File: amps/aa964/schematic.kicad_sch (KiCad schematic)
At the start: 69 parts, among them SW1 AC sw, SW2 gnd sw

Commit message: Fix: the drawn tone stacks now are the tone stack the lab plots, and a gate says so
The tone-stack lab solves one network — the FMV stack documented in
site/src/lib/tonestack.js — and fills its values from each amp's BOM by
reference designator. Nothing checked that the schematic drew those
designators into that network, and nine of the nine drawings did not.

What the drawings said, rebuilt from the committed .kicad_sch files rather
than from the generators:

- 5F6-A, JTM45, 1987, 1959 and 5F4 ran the treble capacitor off the slope
  resistor's FOOT instead of the stack input, and landed the treble pot's
  lower lug on the bass-capacitor node instead of the slope foot.
- Every three-knob drawing left the bass pot's wiper unwired, so the plotted
  output (treble wiper AND bass wiper) existed on no drawing.
- JTM45, 1987 and 1959 put the mid capacitor in series with the mid pot down
  to ground rather than from the slope foot to the mid leg's top.
- 5F6 tied its bass pot as a rheostat and fed the mid capacitor to the middle
  pot's wiper.
- The blackface circuits left the treble pot's lower lug on the bass-cap node
  and tied the bass wiper to its own lug; AB763 drew its 0.047 µF inline on
  top of the bass pot's lug.

The 5F6-A's own layout.yaml — redrawn from the published Fender 5F6-A layout
sheet — already wires the canonical network (treble low to the slope node,
both wipers to the phase-inverter coupler), and 5F4's does too, so the
drawings were corrected to that rather than the lab to the drawings.

Consequences beyond the wires:

- 5F6-A's parts list prints one 0.02 µF line covering the bass and middle
  positions; the drawing showed one capacitor where the circuit has two.
  Added C5b with the same value and the same printed line cited. The plotted
  curve does not move — both positions already used that value.
- The blackface stacks keep the capacitor that feeds the mid leg. With the
  lug corrected, CBN/CB1 (0.1 µF) feeds the bass pot and CBN2/CB2 (0.047 µ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
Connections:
- net at VRT.2 (W), VRV.1: now also VRB.2 (W)
- net at CB1.2, VRB.1: no longer VRB.2 (W), VRT.3
- net at CB1.1, CB2.1, RS.2: now also VRT.3
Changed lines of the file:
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@@
   (wire (pts (xy 77.81 56.9) (xy 84 56.9))
+    (stroke (width 0) (type default)))
+  (wire (pts (xy 96 50.52) (xy 84 50.52))
+    (stroke (width 0) (type default)))
+  (wire (pts (xy 84 50.52) (xy 84 56.9))
     (stroke (width 0) (type default)))
   (symbol (lib_id "cx:C") (at 90 56.9 90) (unit 1)
@@
   (wire (pts (xy 93.81 56.9) (xy 96 56.9))
     (stroke (width 0) (type default)))
-  (wire (pts (xy 96 50.52) (xy 96 56.9))
-    (stroke (width 0) (type default)))
   (symbol (lib_id "cx:POT") (at 96 60.71 0) (unit 1)
     (in_bom yes) (on_board yes)
     (property "Reference" "VRB" (at 98.2 57.51 0) (effects (font (size 1.27 1.27)) (justify left)))
     (property "Value" "250k bass" (at 98.2 59.91 0) (effects (font (size 1.27 1.27)) (justify left))))
-  (junction (at 96 56.9) (diameter 0) (color 0 0 0 0))
-  (wire (pts (xy 101.08 60.71) (xy 105 60.71))
+  (wire (pts (xy 101.08 60.71) (xy 108 60.71))
     (stroke (width 0) (type default)))
-  (wire (pts (xy 105 60.71) (xy 105 53.9))
+  (wire (pts (xy 108 60.71) (xy 108 46.71))
     (stroke (width 0) (type default)))
-  (wire (pts (xy 105 53.9) (xy 96 53.9))
-    (stroke (width 0) (type default)))
-  (junction (at 96 53.9) (diameter 0) (color 0 0 0 0))
+  (junction (at 108 46.71) (diameter 0) (color 0 0 0 0))
   (wire (pts (xy 84 56.9) (xy 84 64.52))
     (stroke (width 0) (type default)))

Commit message: Fix: the published sheets draw a different tone stack, and now we draw theirs
The tone-stack pass rewired nine schematics to one "canonical FMV" network —
treble lower lug on the slope foot, treble and bass wipers joined at the
output, mid cap on a rheostat-wired mid pot — on the strength of the 5F6-A
layout.yaml, a redraw that omits the tone capacitors "for legibility" and
whose stack runs were convention, not sheet reading. Fetching the published
drawings and reading them settles what they actually draw, and it is not that
network. Five sheets were read at 300-400 dpi:

- Fender 5F6 (F-EG), schematic AND factory layout pages
- Fender 5F6-A (I-EG), schematic and layout, side by side
- Marshall JTM45 trem ('types 1961, 1962, 1987/T'), Unicord 70-19-11 (1987),
  and the 100 W Type #2 c.1967 (1959)
- Fender Princeton AA964, schematic and factory layout

All of them agree on a ladder: the treble cap and the slope resistor both
leave the stack input; the first bass cap lands on the node shared by the
treble pot's LOWER lug and the bass pot — the treble pot's cold end sits on
the far side of that capacitor, not on the slope foot; the bass pot is a
rheostat (arrow-through-body on most sheets; the JTM45 loops its wiper to the
foot lug, the 5F6 factory layout straps it into the treble-lug node) in
series down the ladder; the mid cap feeds the MIDDLE POT'S WIPER, not its
top; and the stack's output is the treble wiper ALONE. The blackface AA964
draws the same ladder with its 6.8k fixed leg. The 5F6's presence-in-the-
ground-leg arrangement is unchanged and was always right.

So five drawings return to their sheets: 5f6 and aa964 revert to their
pre-rewire wiring (which the extractor confirms matched the sheets all
along), and jtm45/m1987/m1959 are redrawn to the sheets outright — their old
drawings were wrong differently (treble cap off the slope foot, mid cap in
series to ground, bass wiper floating), so neither old nor "canonical" would
do.

The lab keeps all five as prese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
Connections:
- net at CB1.1, CB2.1, RS.2: no longer VRT.3
- net at CB1.2, VRB.1: now also VRB.2 (W), VRT.3
- net at VRT.2 (W), VRV.1: no longer VRB.2 (W)
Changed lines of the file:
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@@
   (wire (pts (xy 77.81 56.9) (xy 84 56.9))
-    (stroke (width 0) (type default)))
-  (wire (pts (xy 96 50.52) (xy 84 50.52))
-    (stroke (width 0) (type default)))
-  (wire (pts (xy 84 50.52) (xy 84 56.9))
     (stroke (width 0) (type default)))
   (symbol (lib_id "cx:C") (at 90 56.9 90) (unit 1)
@@
   (wire (pts (xy 93.81 56.9) (xy 96 56.9))
     (stroke (width 0) (type default)))
+  (wire (pts (xy 96 50.52) (xy 96 56.9))
+    (stroke (width 0) (type default)))
   (symbol (lib_id "cx:POT") (at 96 60.71 0) (unit 1)
     (in_bom yes) (on_board yes)
@@
   (wire (pts (xy 101.08 60.71) (xy 108 60.71))
     (stroke (width 0) (type default)))
-  (wire (pts (xy 108 60.71) (xy 108 46.71))
+  (wire (pts (xy 108 60.71) (xy 108 56.9))
     (stroke (width 0) (type default)))
-  (junction (at 108 46.71) (diameter 0) (color 0 0 0 0))
+  (wire (pts (xy 108 56.9) (xy 96 56.9))
+    (stroke (width 0) (type default)))
+  (junction (at 96 56.9) (diameter 0) (color 0 0 0 0))
   (wire (pts (xy 84 56.9) (xy 84 64.52))
     (stroke (width 0) (type default)))

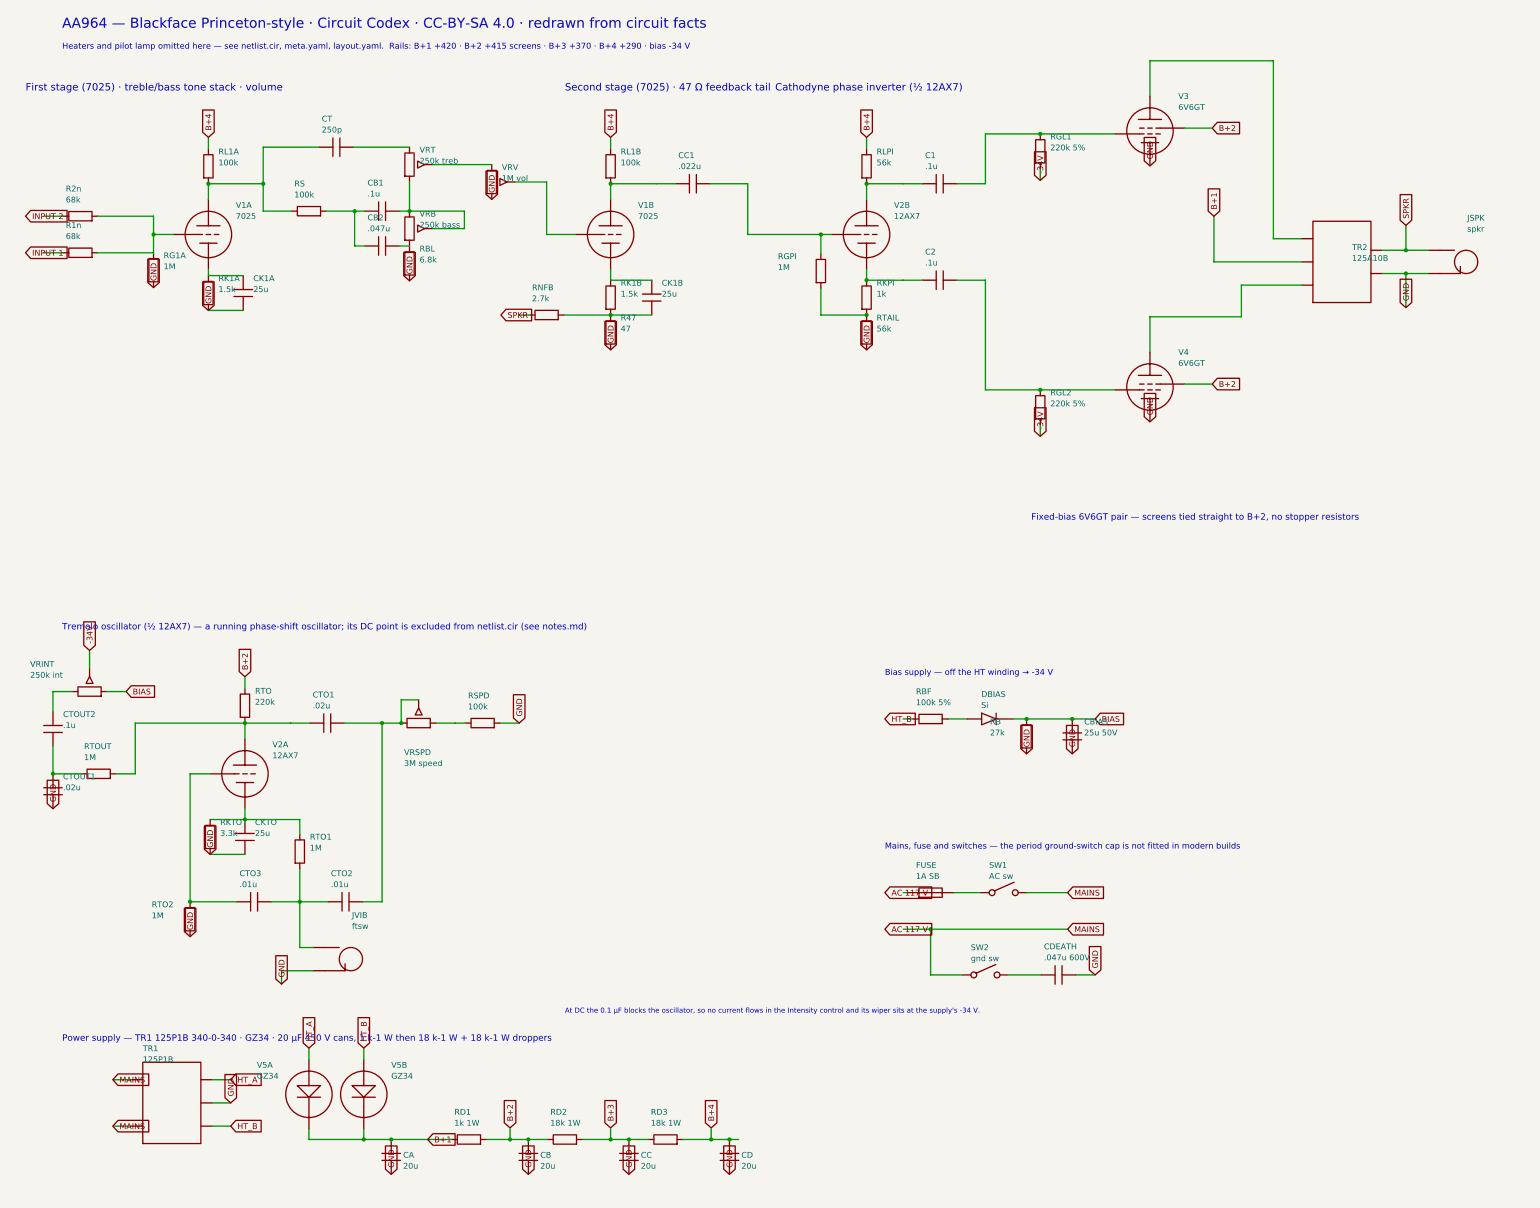
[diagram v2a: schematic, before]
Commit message: Fix: schematic sheets — real title block, fitted paper, no lettering through circuitry
Every sheet in the corpus shipped with an EMPTY title block ("Title:" and
"Date:" blank, default "Sheet /" furniture) laid onto a fixed A4/A3 page
regardless of the drawing's size, with prose annotations placed by hand
wherever a coordinate looked free when the amp was first drawn. The result
read as an unfinished alpha under a `verified` badge: KiCanvas's default view
is `zoom_to_page()`, so a 150 x 110 mm circuit on an A3 sheet opened as a
postage stamp, and later edits had pushed live circuitry under the prose.

schematic_lib.py — the builder now records each element as a (kind, points,
extra) tuple instead of a finished string, so `write()` can measure and move
what it emits:

- emits a real `(title_block …)` read from the amp's own meta.yaml — Title =
  designation + style, Date = the verification (or added) date, Rev = the
  verification status, Company = Circuit Codex, plus the licence and source
  URL as comments. Fixes all 34 sheets from one place;
- emits `(paper "User" w h)` cut to the drawing, translated to a fixed margin,
  with the bottom 34 mm strip reserved for the worksheet's title block. Sheet
  utilisation of the drawable area went from as low as ~20% to 92-98%;
- `note()` queues prose into a wrapped band under the circuit, and `caption()`
  places a section heading over the block it names, nudging it clear if it
  would print through anything;
- per-symbol default label offsets (the old single default printed every pot's
  value through its own wiper arrow and every transformer's designator through
  its body), plus `place_labels()`, which moves any designator/value block that
  would print over ink;
- transformers and chokes are drawn, not boxed: iron core between two windings,
  centre taps where the part has them, and an optional `spec` lettering slot for
  a ratio or impedance;
- `gnd()` takes a direction, because a flag defaulting to "down" at the HEAD of
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
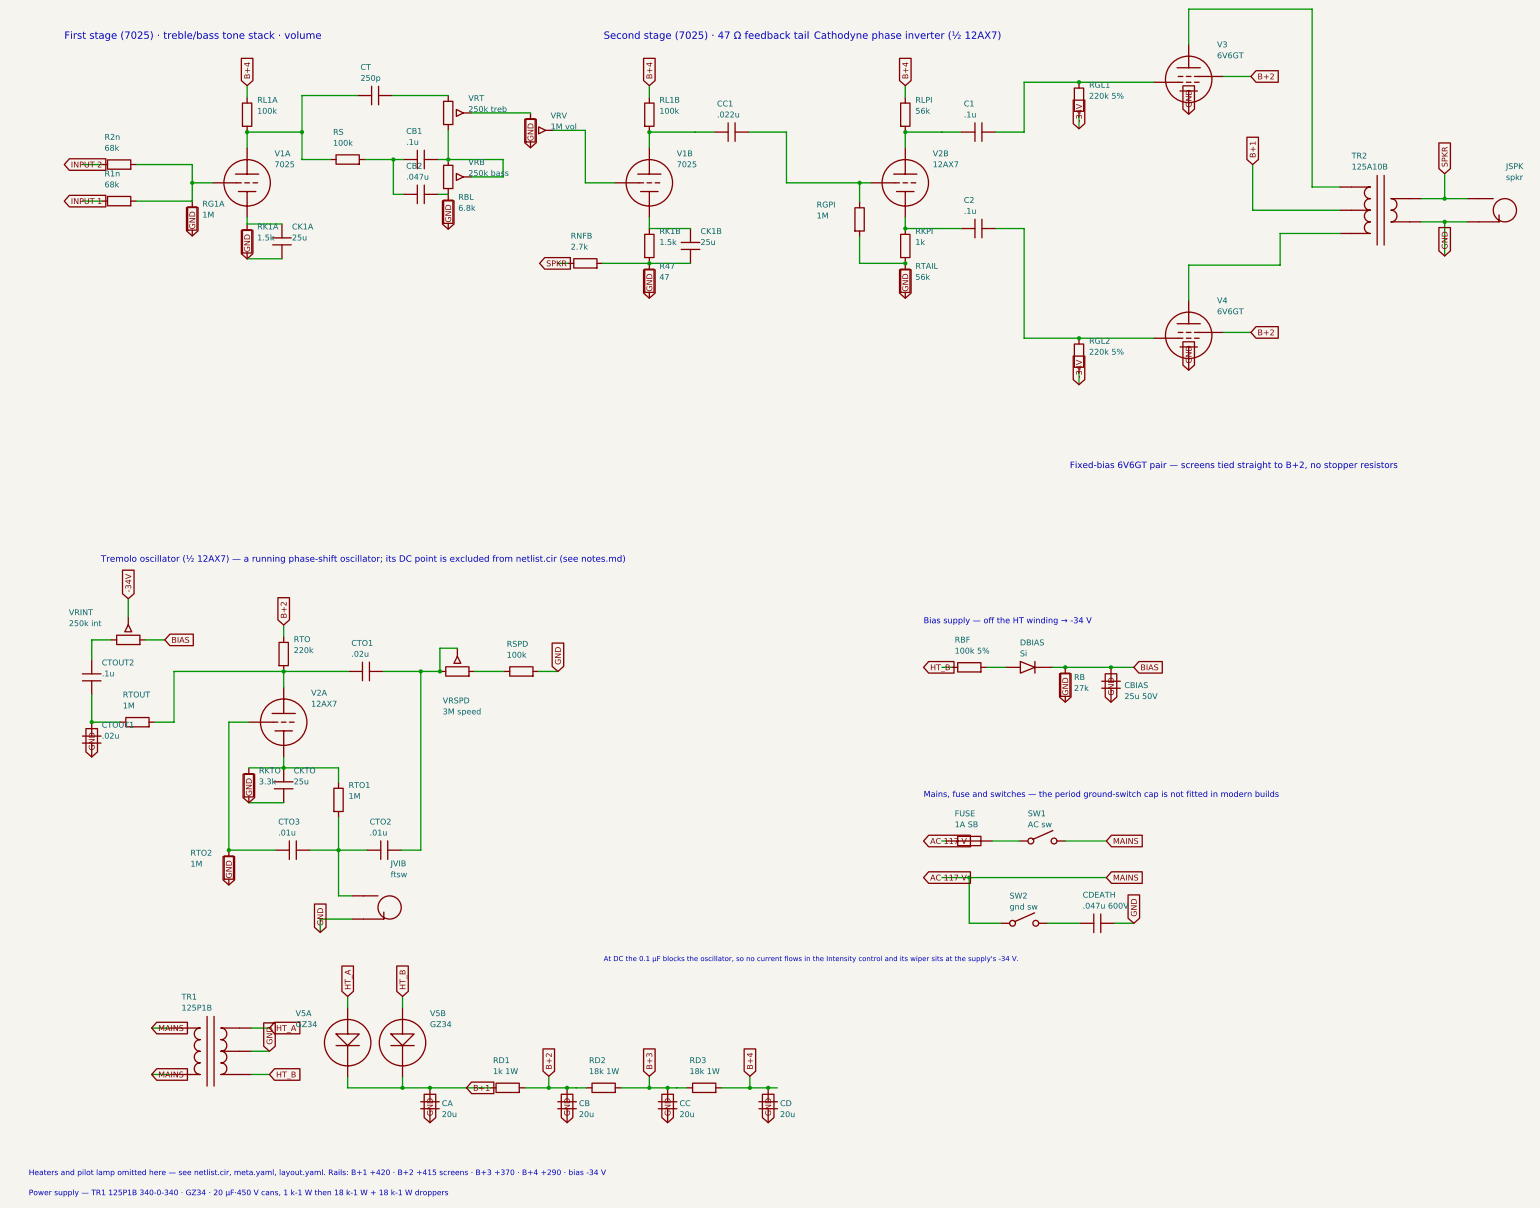
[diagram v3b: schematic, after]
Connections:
- net at VRB.1, VRB.2 (W), VRT.3: no longer CB1.2
- net at RBL.1, VRB.3: no longer CB2.2
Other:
- note removed: "AA964 — Blackface Princeton-style · Circuit Codex · CC-BY-SA 4.0 · redrawn from circuit facts"
- company: (none) -> Circuit Codex
- title: (none) -> AA964 — Blackface Princeton-style
